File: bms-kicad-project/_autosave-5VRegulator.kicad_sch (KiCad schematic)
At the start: 22 parts, among them U5 SIC461ED-T1-GE3

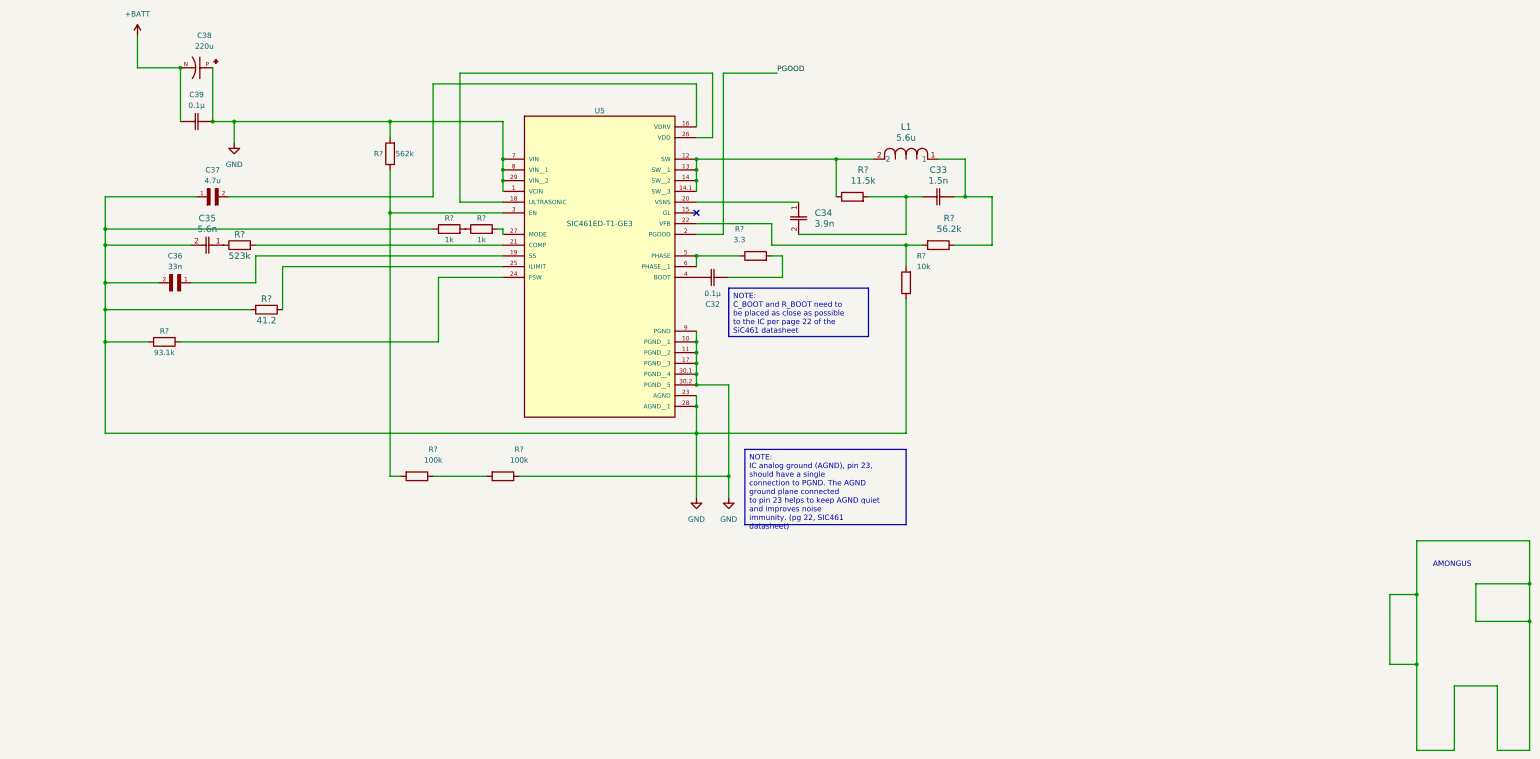
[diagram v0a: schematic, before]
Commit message: feat: Changed all resistor symbols to be the standard KiCAD symbol, started improving schematic.
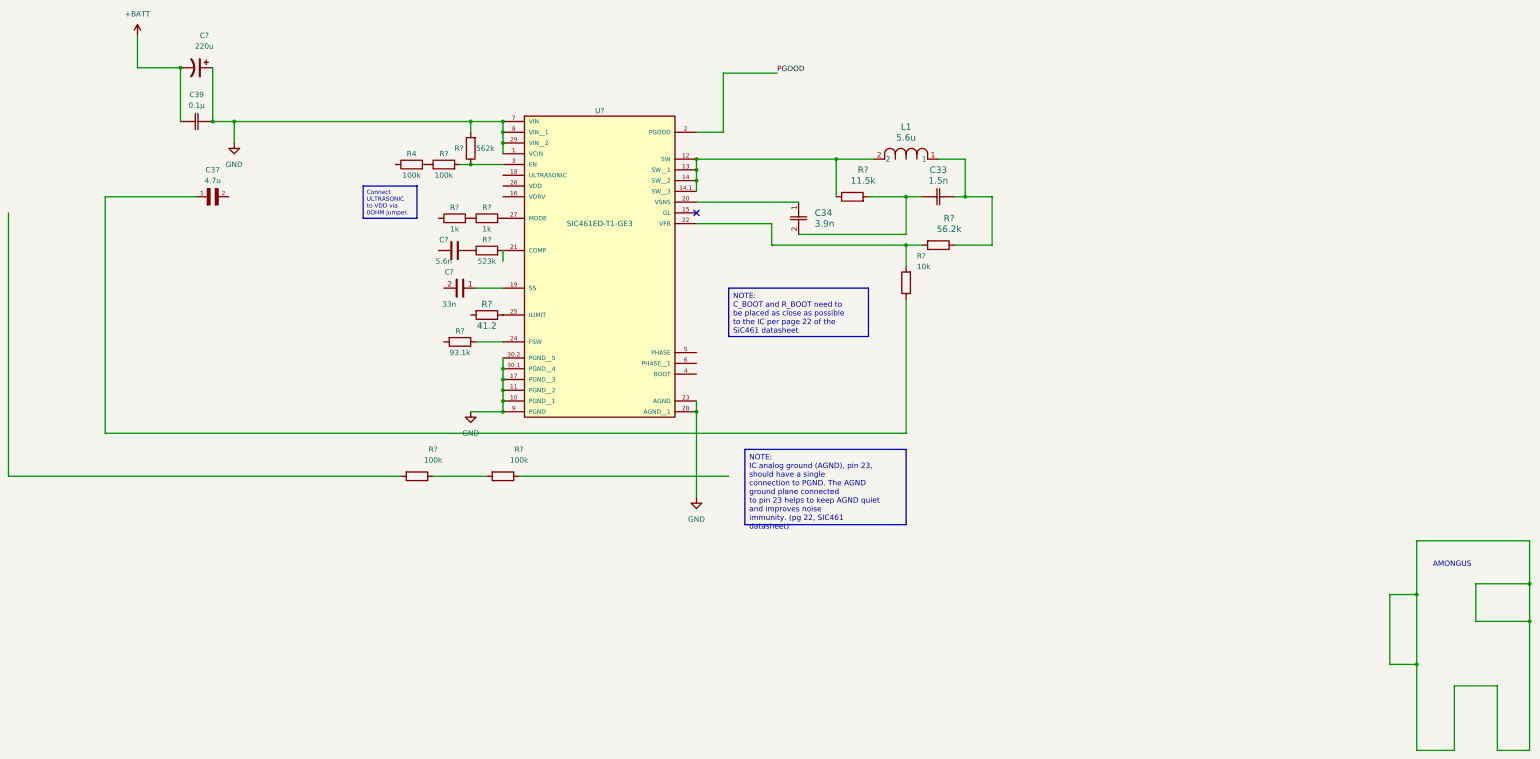
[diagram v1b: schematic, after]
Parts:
- removed C32: 0.1µ, FixedWing:CAP_GCJ-18_MUR, symbol FixedWing:GCJ188R72A104KA01D
- removed R?: 3.3, FixedWing:RESC1608X55N, symbol FixedWing:RK73H1JTTD3R30F
- added R4, R?: 100k, FixedWing:RESC2012X60N, symbol FixedWing:RC0805FR-07100KL
- renumbered C38 to C?, C35 to C?, C36 to C?, U5 to U?
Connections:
- net +BATT: now also C?.2; no longer C?.N
- net GND: now also C?.1; no longer C37.1, C?.2, C?.2, C?.P, R?.1, R?.1, R?.1, R?.2, R?.2
- net at R?.1, U?.3 (EN): now also R?.2; no longer R?.2
- net at U?.5 (PHASE): no longer U?.6 (PHASE__1)
- net at C37.2: no longer U?.16 (VDRV)
- net at U?.18 (ULTRASONIC): no longer U?.26 (VDD)
- new net: C37.1, R?.1
- new net: R4.2, R?.1
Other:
- moved on the sheet: R?
